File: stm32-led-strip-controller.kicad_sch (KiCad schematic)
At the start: 45 parts, among them J101 Tag Connector, J102 Barrel_Jack_Switch, J104 JST 2.54 Header, J106 JST 2.54 Header, SW101 SW_DIP_x04, SW106 SW_Push, U101 STM32F401RCTx, U102 74AHCT1G125, U102 USBLC6-2SC6, U104 M24C64-RMN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

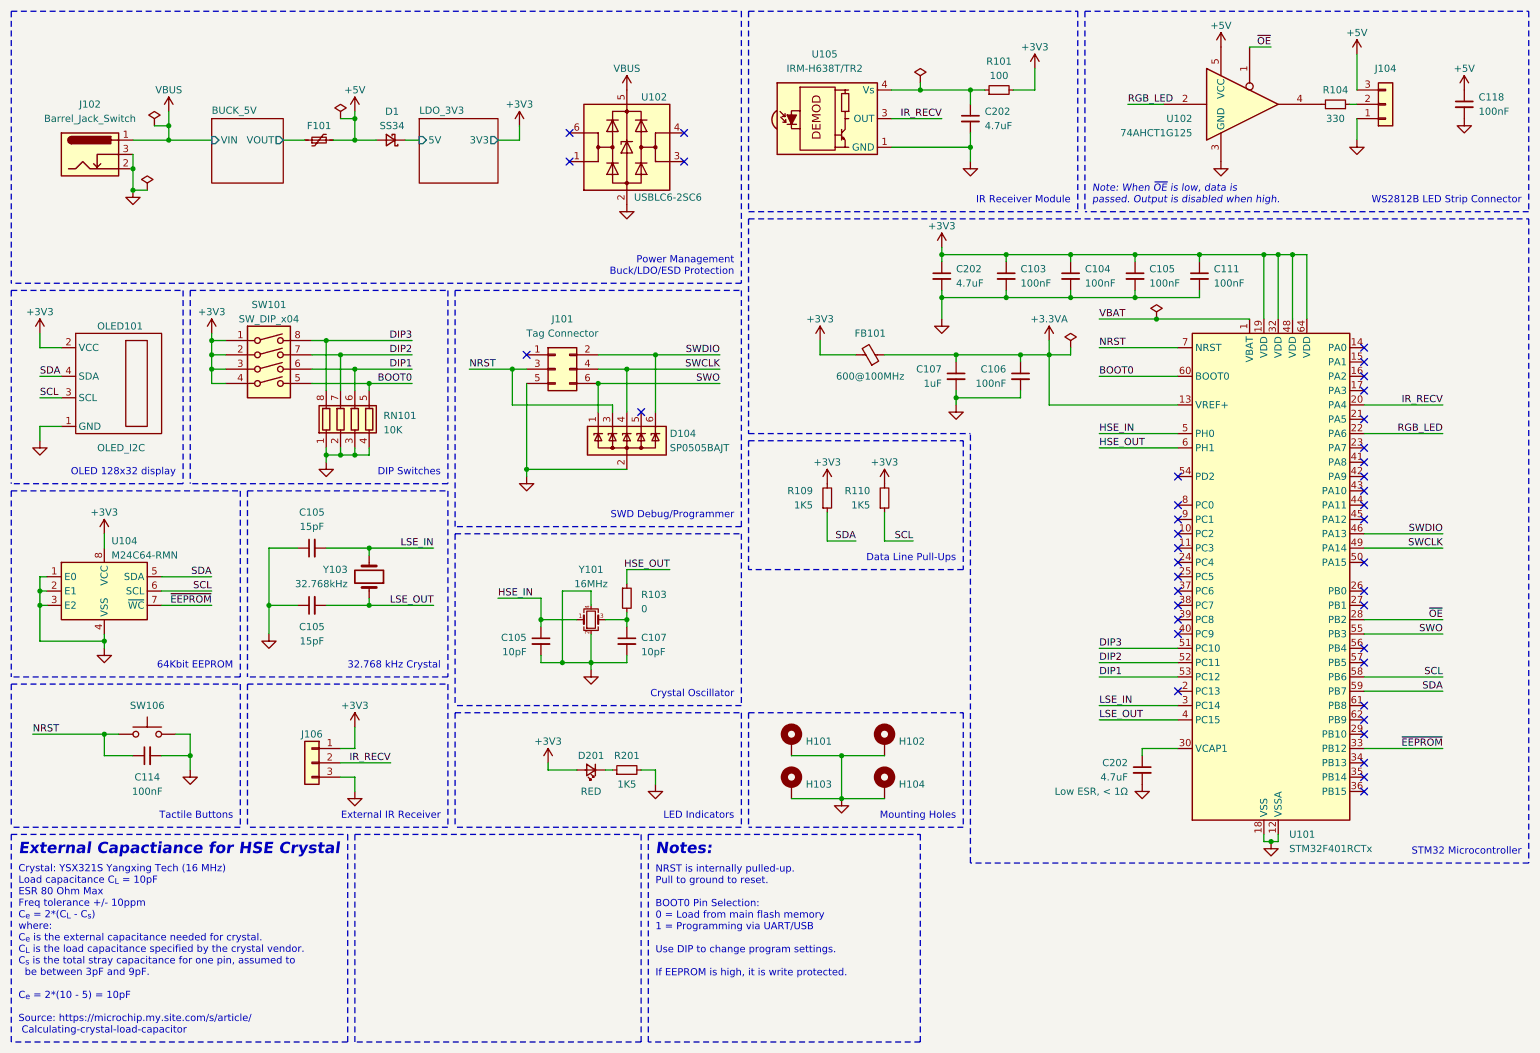
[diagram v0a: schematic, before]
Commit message: change footprint, remove DIP switch
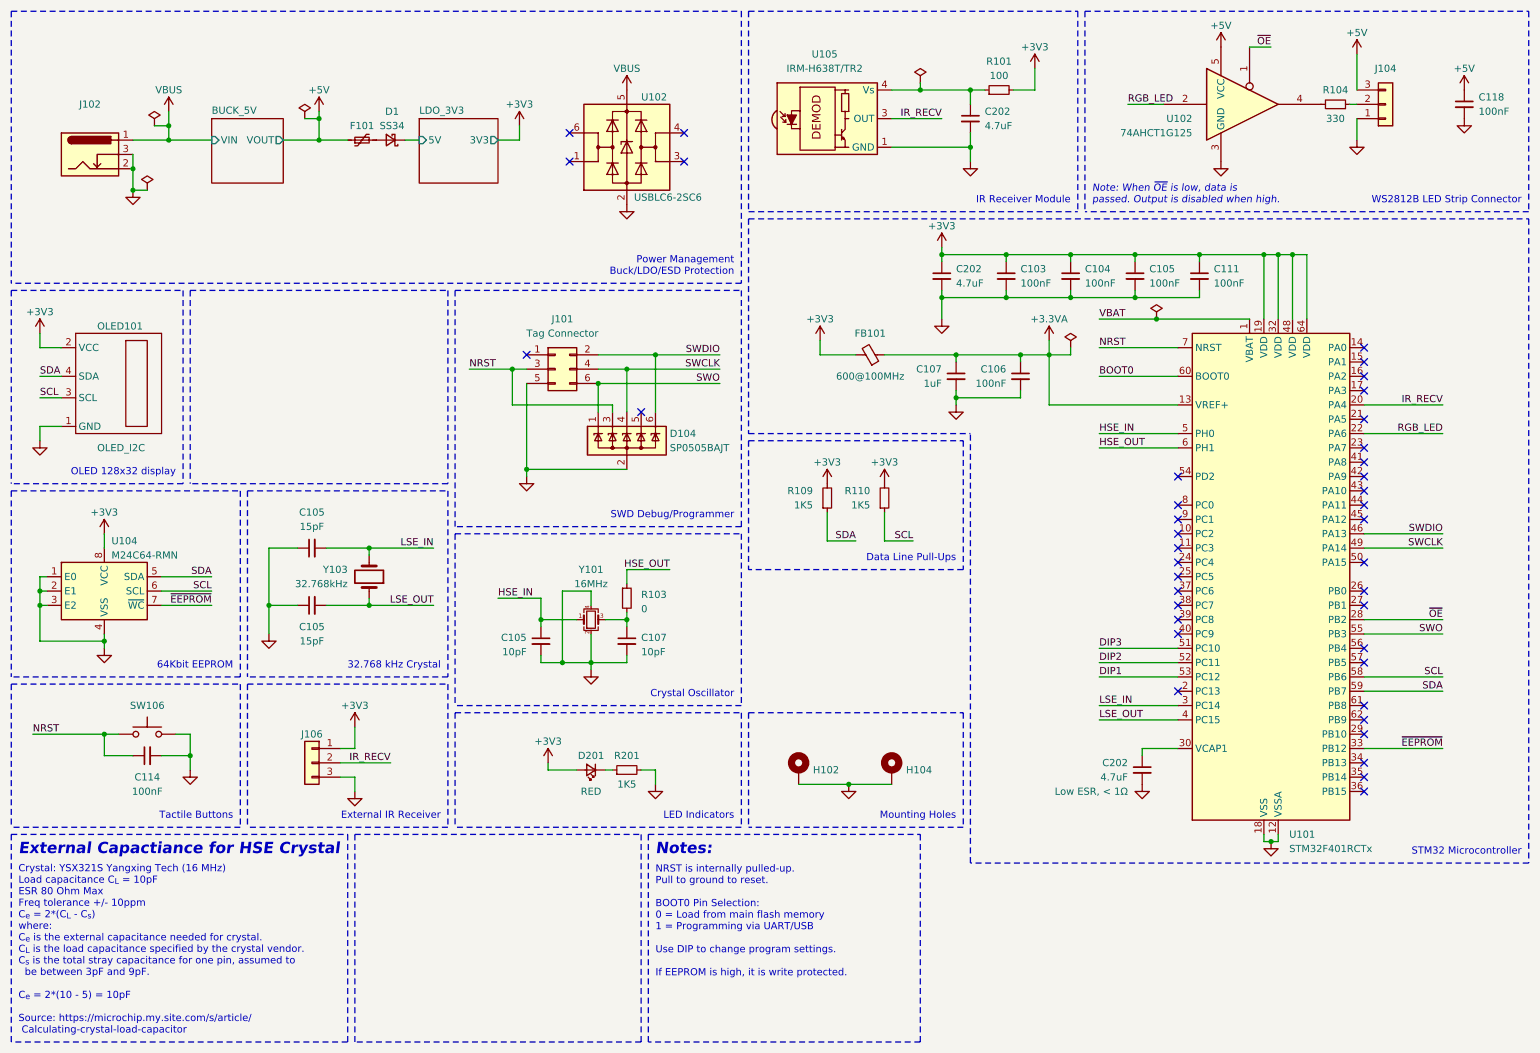
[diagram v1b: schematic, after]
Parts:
- removed H101, H103: MountingHole, MountingHole:MountingHole_3.2mm_M3_Pad_Via, symbol Mechanical:MountingHole_Pad
- removed RN101: 10K, Resistor_SMD:R_Array_Convex_4x0603, symbol Device:R_Pack04
- removed SW101: SW_DIP_x04, User_Footprint:SMDIP-8_W6.6mm, symbol Switch:SW_DIP_x04
- J102: footprint Connector_BarrelJack:BarrelJack_Wuerth_6941xx301002 -> User_Footprint:BarrelJack_GCT_DCJ250-10-A-K1-K; now left out of the parts list
- J104: footprint Connector_JST:JST_XH_B3B-XH-A_1x03_P2.50mm_Vertical -> Connector_JST:JST_XH_S3B-XH-A-1_1x03_P2.50mm_Horizontal
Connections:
- net BUCK_5V/VOUT is gone; now on net +5V: F101.1
- net +5V: no longer D1.2 (A), F101.2
- new net: D1.2 (A), F101.2
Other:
- note removed: "DIP Switches"
- moved on the sheet: F101, H102, H104
